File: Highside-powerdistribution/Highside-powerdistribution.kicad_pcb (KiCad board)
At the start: 2 copper layers, 78 x 80 mm, 41 parts, among them J10 Screw_Terminal_01x02, J11 Screw_Terminal_01x02, J12 Screw_Terminal_01x02, J13 Screw_Terminal_01x02, J14 Conn_01x02, J15 Screw_Terminal_01x06, J8 Screw_Terminal_01x02, J9 Screw_Terminal_01x02, Q1 P-MOSFET, Q2 P-MOSFET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

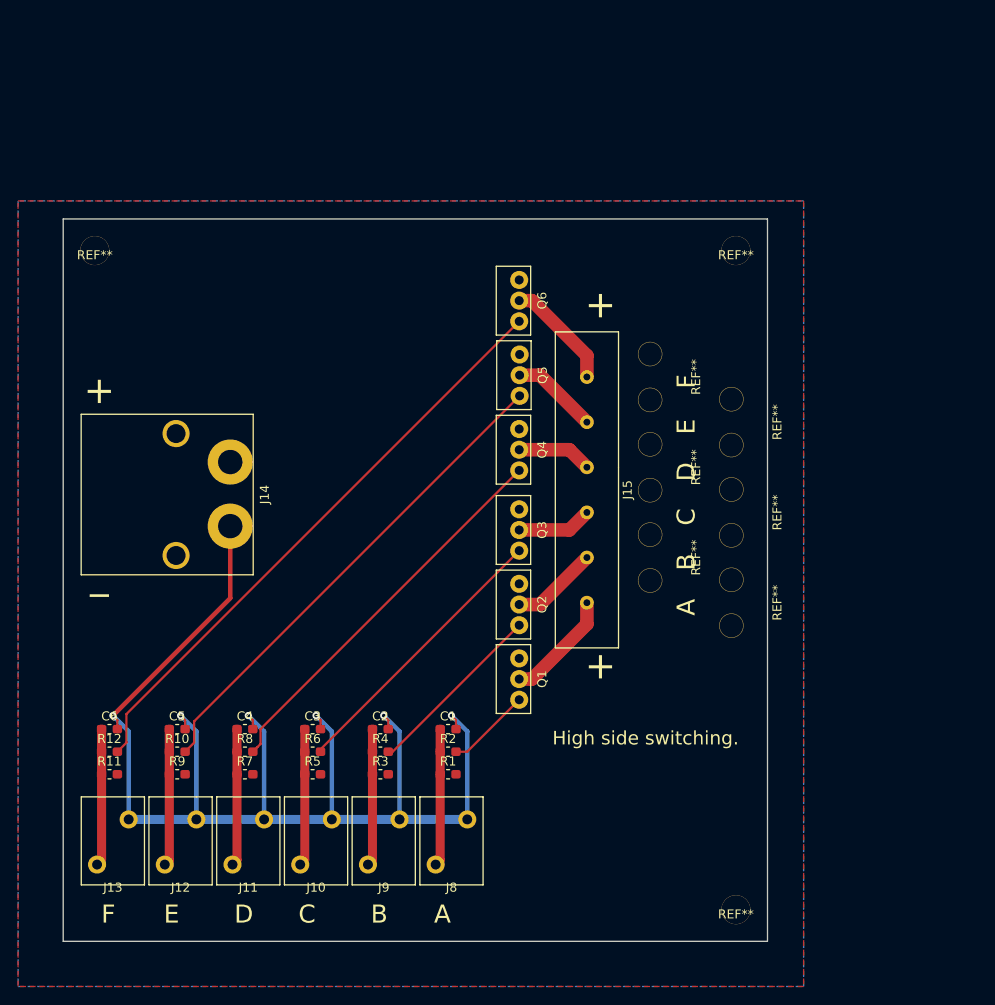
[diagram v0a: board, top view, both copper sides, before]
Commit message: Added 5x20 fuses on PCB
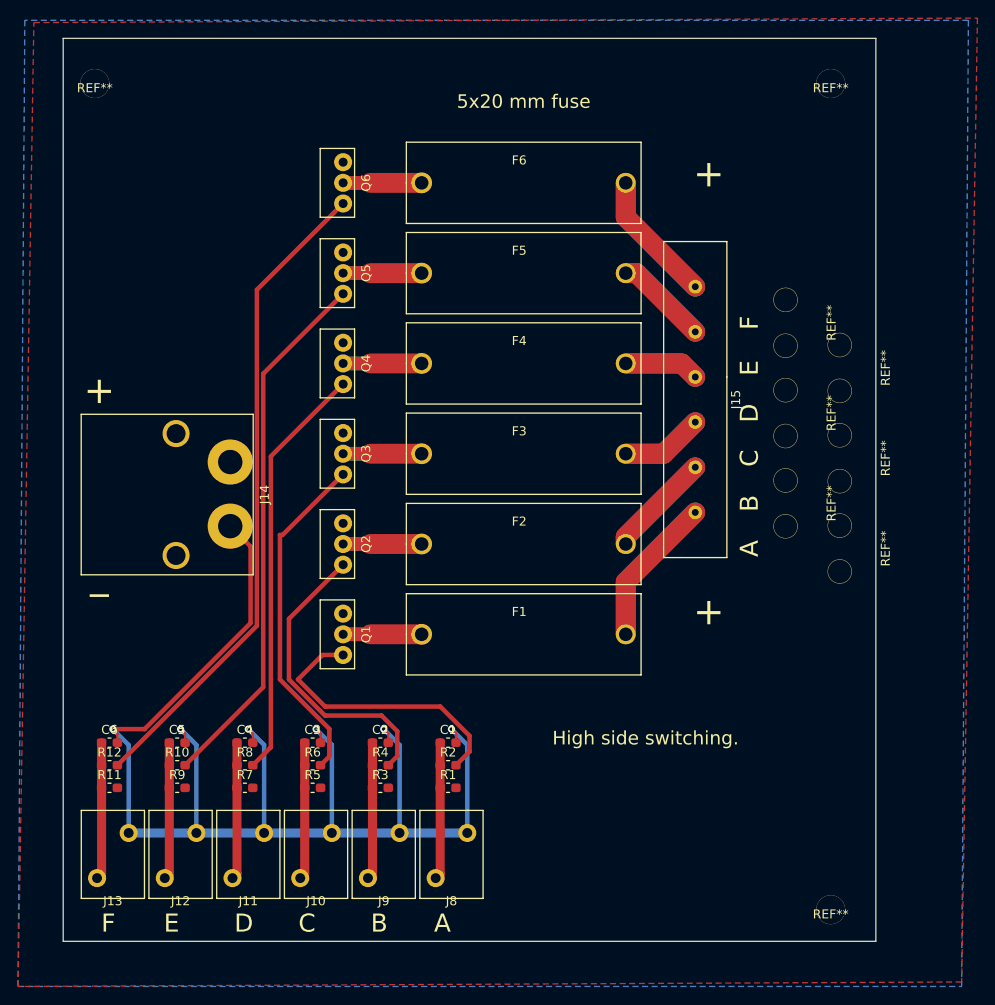
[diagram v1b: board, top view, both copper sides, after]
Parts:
- added F1: Fuse, Highside-powerdistribution:PTF-15, F.Cu at (101.0, 116.0)
- added F2: Fuse, Highside-powerdistribution:PTF-15, F.Cu at (101.0, 106.0)
- added F3: Fuse, Highside-powerdistribution:PTF-15, F.Cu at (101.0, 96.0)
- added F4: Fuse, Highside-powerdistribution:PTF-15, F.Cu at (101.0, 86.0)
- added F5: Fuse, Highside-powerdistribution:PTF-15, F.Cu at (101.0, 76.0)
- added F6: Fuse, Highside-powerdistribution:PTF-15, F.Cu at (101.0, 66.0)
- moved Q6 23.5 mm to (81.0, 66.0)
- moved Q5 22.6 mm to (81.0, 76.0)
- moved Q4 21.7 mm to (81.0, 86.0)
- moved REF** 21.3 mm to (135.0, 55.0)
- moved Q3 21.3 mm to (81.0, 96.0)
- moved Q2 20.6 mm to (81.0, 106.0)
- moved Q1 20.1 mm to (81.0, 116.0)
- moved REF** 18.5 mm to (53.5, 55.0)
- moved REF** 16.2 mm to (130.0, 101.5)
- moved REF** 16.2 mm to (130.0, 91.5)
- moved REF** 16.2 mm to (130.0, 81.5)
- moved J15 15.6 mm to (120.0, 90.0)
- moved REF** 13.4 mm to (136.0, 106.5)
- moved REF** 13.4 mm to (136.0, 96.5)
- moved REF** 13.4 mm to (136.0, 86.5)
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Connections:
- J15 pad 1: SSR-A -> Net-(F1-Pad1)
- J15 pad 2: SSR-B -> Net-(F2-Pad1)
- J15 pad 3: SSR-C -> Net-(F3-Pad1)
- J15 pad 4: SSR-D -> Net-(F4-Pad1)
- J15 pad 5: SSR-E -> Net-(F5-Pad1)
- J15 pad 6: SSR-F -> Net-(F6-Pad1)
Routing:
- net Net-(F1-Pad1): track 0.00 -> 33.4 mm
- net Net-(F6-Pad1): track 0.00 -> 29.4 mm
- net Net-(F2-Pad1): track 0.00 -> 23.4 mm
- net Net-(Q1-Pad1): track 9.38 -> 31.6 mm
- net Net-(F5-Pad1): track 0.00 -> 20.8 mm
- net Net-(F3-Pad1): track 0.00 -> 18.3 mm
- net Net-(F4-Pad1): track 0.00 -> 16.6 mm
- net Net-(Q2-Pad1): track 20.3 -> 33.7 mm
- net SSR-D: track 8.31 -> 17.4 mm
- net SSR-C: track 8.31 -> 17.4 mm
- net SSR-E: track 9.60 -> 17.4 mm
- net SSR-B: track 9.65 -> 17.4 mm
- net Net-(Q3-Pad1): track 31.4 -> 38.0 mm
- net Net-(Q6-Pad1): track 66.1 -> 72.6 mm
- net GND: track 147.5 -> 152.9 mm
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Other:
- board size 78 x 80 mm -> 90 x 100 mm
- board text added: "5x20 mm fuse"

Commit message: Added serie connector
To use one switch for multiple MOSFETs. Just a pinheader.
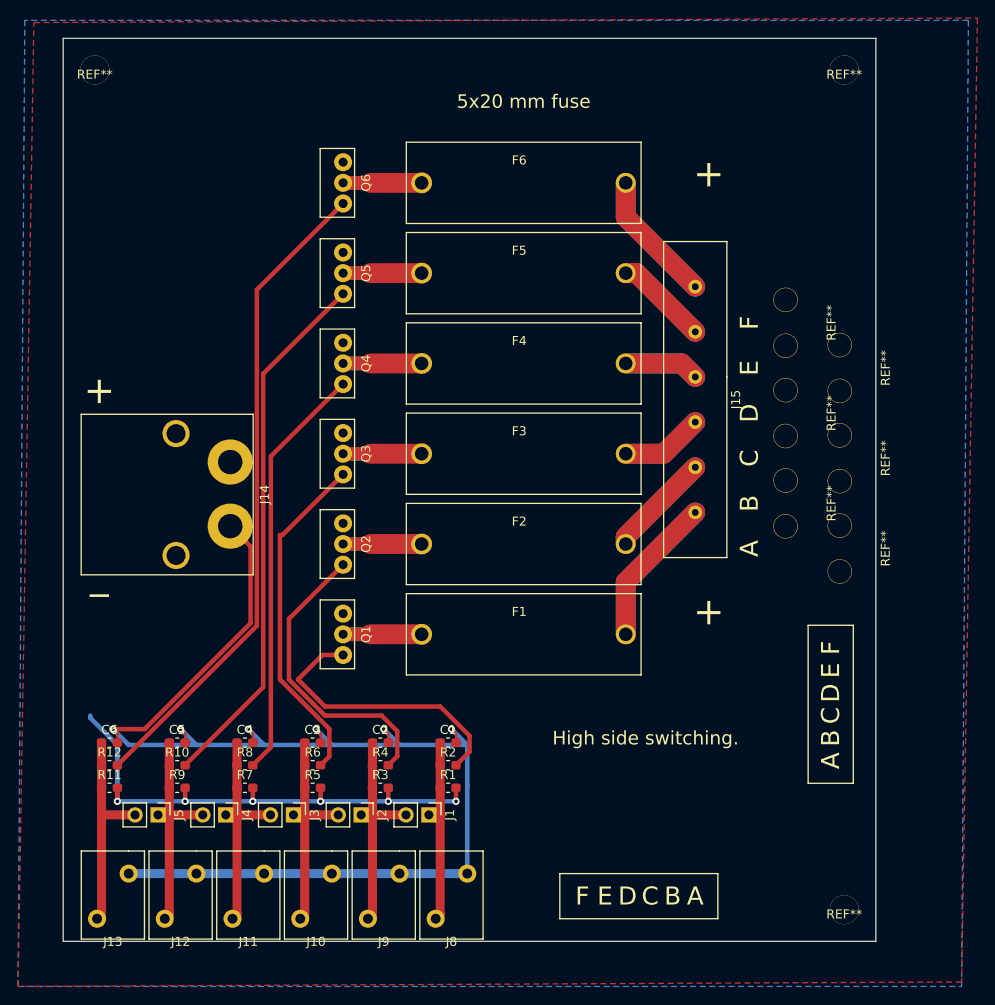
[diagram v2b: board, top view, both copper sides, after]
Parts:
- added J1: Conn_01x02_Male, Connector_PinHeader_2.54mm:PinHeader_1x02_P2.54mm_Vertical, F.Cu at (90.5, 136.0)
- added J2: Conn_01x02_Male, Connector_PinHeader_2.54mm:PinHeader_1x02_P2.54mm_Vertical, F.Cu at (83.0, 136.0)
- added J3: Conn_01x02_Male, Connector_PinHeader_2.54mm:PinHeader_1x02_P2.54mm_Vertical, F.Cu at (75.5, 136.0)
- added J4: Conn_01x02_Male, Connector_PinHeader_2.54mm:PinHeader_1x02_P2.54mm_Vertical, F.Cu at (68.0, 136.0)
- added J5: Conn_01x02_Male, Connector_PinHeader_2.54mm:PinHeader_1x02_P2.54mm_Vertical, F.Cu at (60.5, 136.0)
- moved J10 4.50 mm to (78.0, 147.5)
- moved J11 4.50 mm to (70.5, 147.5)
- moved J12 4.50 mm to (63.0, 147.5)
- moved J13 4.50 mm to (55.5, 147.5)
- moved J8 4.50 mm to (93.0, 147.5)
- moved J9 4.50 mm to (85.5, 147.5)
- moved REF** 2.12 mm to (136.5, 53.5)
- moved REF** 1.50 mm to (53.5, 53.5)
- moved REF** 1.50 mm to (136.5, 146.5)
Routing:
- net +12V: track 0.00 -> 57.2 mm, vias 0 -> 6
- net Net-(C4-Pad1): track 15.2 -> 26.0 mm
- net Net-(C2-Pad1): track 15.2 -> 26.0 mm
- net Net-(C5-Pad1): track 15.2 -> 24.7 mm
- net Net-(C3-Pad1): track 15.2 -> 24.7 mm
- net Net-(C6-Pad1): track 15.2 -> 23.5 mm
- net GND: track 152.9 -> 146.1 mm
- net Net-(C1-Pad1): track 15.2 -> 21.1 mm

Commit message: Finished Rev 1.0
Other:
- board text added: "Positive switches with 5x20 fuses. High side switching with P-channel MOSFET."
- board text added: "Rev 1.0 2019-11-18"
- board text removed: "High side switching."
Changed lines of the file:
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@@
   (general
     (thickness 1.6)
-    (drawings 36)
+    (drawings 37)
     (tracks 174)
     (zones 0)
@@
     )
   )
+  (gr_text "Rev 1.0\n2019-11-18" (at 65 55) (layer F.SilkS)
+    (effects (font (size 1 1) (thickness 0.15)))
+  )
   (gr_line (start 132.5 115) (end 137.5 115) (layer F.SilkS) (width 0.12))
   (gr_line (start 137.5 115) (end 137.5 132.5) (layer F.SilkS) (width 0.12))
@@
     (effects (font (size 3 3) (thickness 0.3)))
   )
-  (gr_text "High side switching." (at 114.5 127.5) (layer F.SilkS)
-    (effects (font (size 1.5 1.5) (thickness 0.3)))
+  (gr_text "Positive switches with 5x20 fuses. \nHigh side switching with P-channel MOSFET." (at 117.5 137.5) (layer F.SilkS)
+    (effects (font (size 1 1) (thickness 0.15)))
   )
   (gr_text F (at 126 81.5 90) (layer F.SilkS)
@@
     (polygon
       (pts
-        (xy 49.5 125.5) (xy 97.208579 125.5) (xy 97.5 150.5) (xy 48.917157 150.218842)
+        (xy 50 125.5) (xy 97 125.5) (xy 97 150) (xy 50 150)
       )
     )

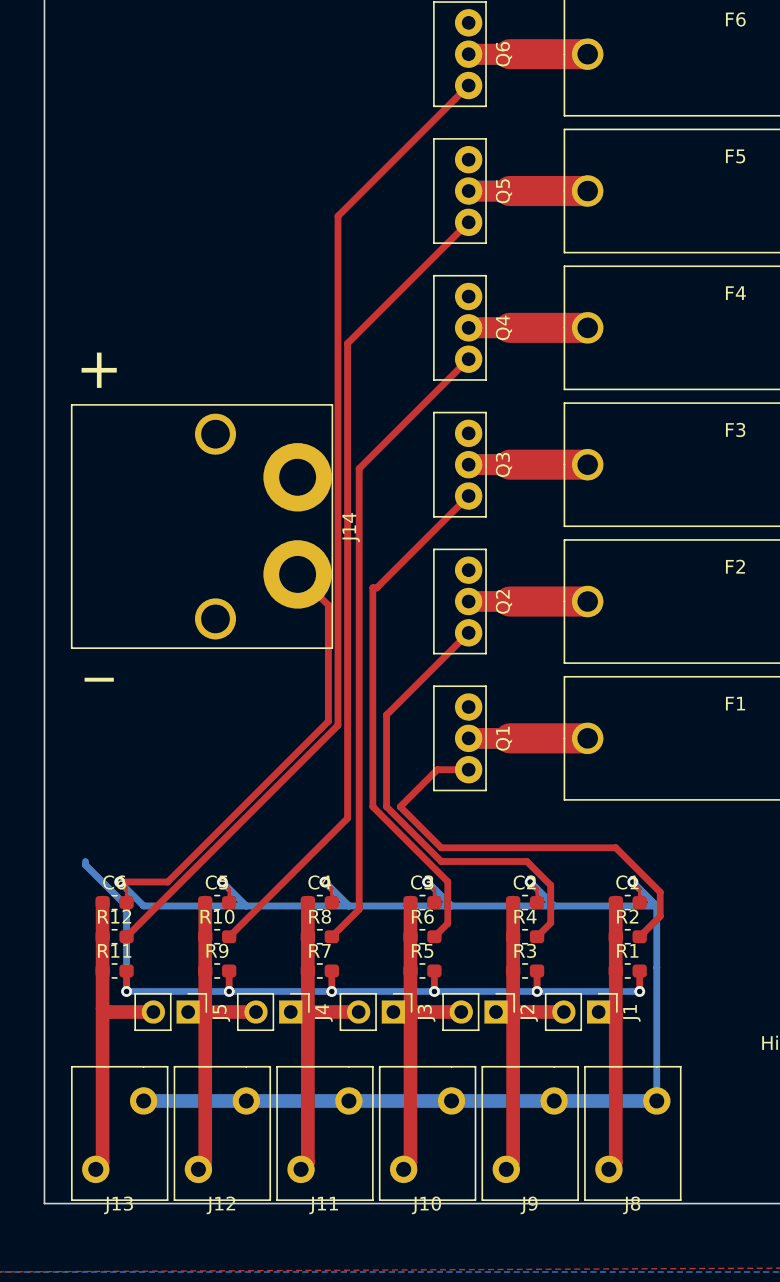
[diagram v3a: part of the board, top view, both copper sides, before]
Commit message: Routed updated with LP filter
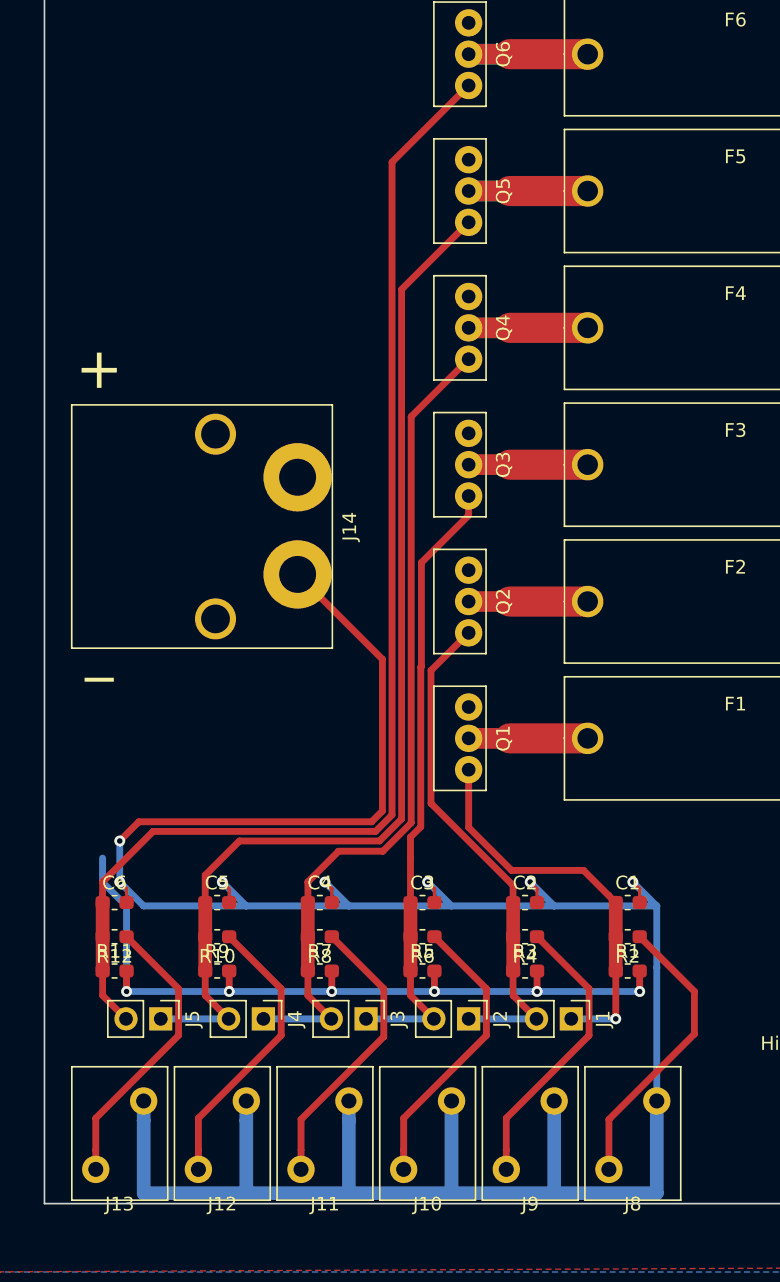
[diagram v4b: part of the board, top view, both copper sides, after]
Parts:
- moved J1 2.06 mm to (88.5, 136.5)
- moved J2 2.06 mm to (81.0, 136.5)
- moved J3 2.06 mm to (73.5, 136.5)
- moved J4 2.06 mm to (66.0, 136.5)
- moved J5 2.06 mm to (58.5, 136.5)
- turned R10 to 180 degrees
- turned R12 to 180 degrees
- turned R2 to 180 degrees
- turned R4 to 180 degrees
- turned R6 to 180 degrees
- turned R8 to 180 degrees
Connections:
- J10 pad 1: Net-(C3-Pad1) -> Net-(J10-Pad1)
- J11 pad 1: Net-(C4-Pad1) -> Net-(J11-Pad1)
- J12 pad 1: Net-(C5-Pad1) -> Net-(J12-Pad1)
- J13 pad 1: Net-(C6-Pad1) -> Net-(J13-Pad1)
- J8 pad 1: Net-(C1-Pad1) -> Net-(J8-Pad1)
- J9 pad 1: Net-(C2-Pad1) -> Net-(J9-Pad1)
- Q1 pad 1: Net-(Q1-Pad1) -> Net-(C1-Pad1)
- Q2 pad 1: Net-(Q2-Pad1) -> Net-(C2-Pad1)
- Q3 pad 1: Net-(Q3-Pad1) -> Net-(C3-Pad1)
- Q4 pad 1: Net-(Q4-Pad1) -> Net-(C4-Pad1)
- Q5 pad 1: Net-(Q5-Pad1) -> Net-(C5-Pad1)
- Q6 pad 1: Net-(Q6-Pad1) -> Net-(C6-Pad1)
- R10 pad 1: Net-(C5-Pad1) -> Net-(J12-Pad1)
- R10 pad 2: Net-(Q5-Pad1) -> Net-(C5-Pad1)
- R12 pad 1: Net-(C6-Pad1) -> Net-(J13-Pad1)
- R12 pad 2: Net-(Q6-Pad1) -> Net-(C6-Pad1)
- R2 pad 1: Net-(C1-Pad1) -> Net-(J8-Pad1)
- R2 pad 2: Net-(Q1-Pad1) -> Net-(C1-Pad1)
- R4 pad 1: Net-(C2-Pad1) -> Net-(J9-Pad1)
- R4 pad 2: Net-(Q2-Pad1) -> Net-(C2-Pad1)
- R6 pad 1: Net-(C3-Pad1) -> Net-(J10-Pad1)
- R6 pad 2: Net-(Q3-Pad1) -> Net-(C3-Pad1)
- R8 pad 1: Net-(C4-Pad1) -> Net-(J11-Pad1)
- R8 pad 2: Net-(Q4-Pad1) -> Net-(C4-Pad1)
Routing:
- net Net-(Q6-Pad1): track 72.6 -> 0.00 mm
- net Net-(C6-Pad1): track 23.5 -> 89.5 mm
- net Net-(Q5-Pad1): track 59.5 -> 0.00 mm
- net Net-(C5-Pad1): track 24.7 -> 77.9 mm
- net GND: track 146.1 -> 197.7 mm, vias 6 -> 7
- net Net-(Q4-Pad1): track 46.4 -> 0.00 mm
- net Net-(Q3-Pad1): track 38.0 -> 0.00 mm
- net Net-(C4-Pad1): track 26.0 -> 60.6 mm
- net Net-(Q2-Pad1): track 33.7 -> 0.00 mm
- net Net-(Q1-Pad1): track 31.6 -> 0.00 mm
- net Net-(J8-Pad1): track 0.00 -> 21.2 mm
- net Net-(J13-Pad1): track 0.00 -> 21.1 mm
- net Net-(J9-Pad1): track 0.00 -> 21.1 mm
- net Net-(J12-Pad1): track 0.00 -> 21.1 mm
- net Net-(J11-Pad1): track 0.00 -> 21.1 mm
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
